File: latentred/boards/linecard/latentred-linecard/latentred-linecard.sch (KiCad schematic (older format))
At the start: 0 parts

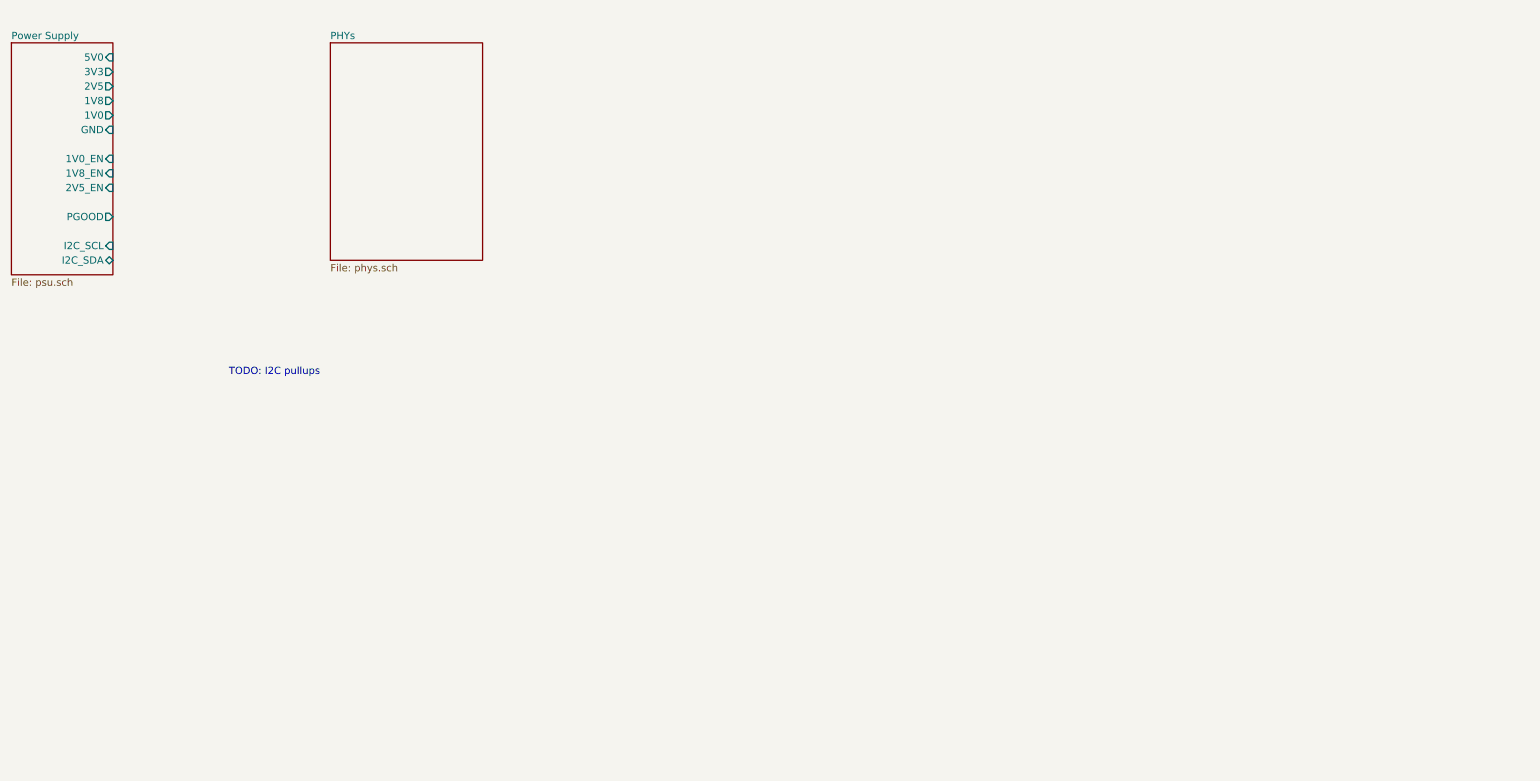
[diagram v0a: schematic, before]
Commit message: Continued work on line card design. Now have PSU and all PHYs, still working on clock distribution.
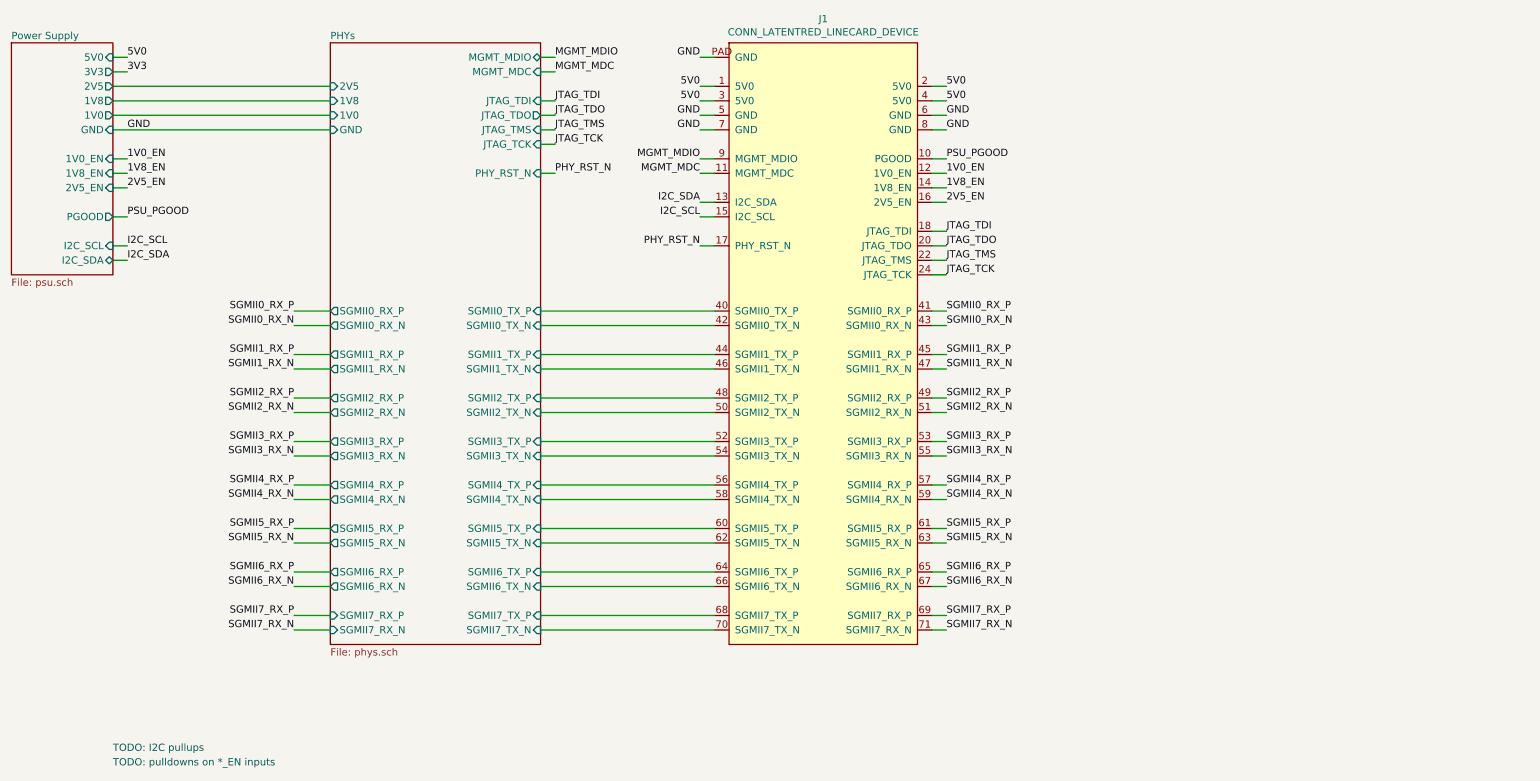
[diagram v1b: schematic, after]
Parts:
- added J1: CONN_LATENTRED_LINECARD_DEVICE, symbol special-azonenberg:CONN_LATENTRED_LINECARD_DEVICE
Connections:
- new net 1V0_EN: J1.12 (1V0_EN)
- new net 1V8_EN: J1.14 (1V8_EN)
- new net 2V5_EN: J1.16 (2V5_EN)
- new net 5V0: J1.1 (5V0), J1.2 (5V0), J1.3 (5V0), J1.4 (5V0)
- new net GND: J1.5 (GND), J1.6 (GND), J1.7 (GND), J1.8 (GND), J1.PAD (GND)
- new net I2C_SCL: J1.15 (I2C_SCL)
- new net I2C_SDA: J1.13 (I2C_SDA)
- new net JTAG_TCK: J1.24 (JTAG_TCK)
- new net JTAG_TDI: J1.18 (JTAG_TDI)
- new net JTAG_TDO: J1.20 (JTAG_TDO)
- new net JTAG_TMS: J1.22 (JTAG_TMS)
- new net MGMT_MDC: J1.11 (MGMT_MDC)
- new net MGMT_MDIO: J1.9 (MGMT_MDIO)
- new net PHY_RST_N: J1.17 (PHY_RST_N)
- new net PHYs/SGMII0_TX_N: J1.42 (SGMII0_TX_N)
- new net PHYs/SGMII0_TX_P: J1.40 (SGMII0_TX_P)
- new net PHYs/SGMII1_TX_N: J1.46 (SGMII1_TX_N)
- new net PHYs/SGMII1_TX_P: J1.44 (SGMII1_TX_P)
- new net PHYs/SGMII2_TX_N: J1.50 (SGMII2_TX_N)
- new net PHYs/SGMII2_TX_P: J1.48 (SGMII2_TX_P)
- new net PHYs/SGMII3_TX_N: J1.54 (SGMII3_TX_N)
- new net PHYs/SGMII3_TX_P: J1.52 (SGMII3_TX_P)
- new net PHYs/SGMII4_TX_N: J1.58 (SGMII4_TX_N)
- new net PHYs/SGMII4_TX_P: J1.56 (SGMII4_TX_P)
- new net PHYs/SGMII5_TX_N: J1.62 (SGMII5_TX_N)
- new net PHYs/SGMII5_TX_P: J1.60 (SGMII5_TX_P)
- new net PHYs/SGMII6_TX_N: J1.66 (SGMII6_TX_N)
- new net PHYs/SGMII6_TX_P: J1.64 (SGMII6_TX_P)
- new net PHYs/SGMII7_TX_N: J1.70 (SGMII7_TX_N)
- new net PHYs/SGMII7_TX_P: J1.68 (SGMII7_TX_P)
- new net PSU_PGOOD: J1.10 (PGOOD)
- new net SGMII0_RX_N: J1.43 (SGMII0_RX_N)
- new net SGMII0_RX_P: J1.41 (SGMII0_RX_P)
- new net SGMII1_RX_N: J1.47 (SGMII1_RX_N)
- new net SGMII1_RX_P: J1.45 (SGMII1_RX_P)
- new net SGMII2_RX_N: J1.51 (SGMII2_RX_N)
- new net SGMII2_RX_P: J1.49 (SGMII2_RX_P)
- new net SGMII3_RX_N: J1.55 (SGMII3_RX_N)
- new net SGMII3_RX_P: J1.53 (SGMII3_RX_P)
- new net SGMII4_RX_N: J1.59 (SGMII4_RX_N)
- new net SGMII4_RX_P: J1.57 (SGMII4_RX_P)
- new net SGMII5_RX_N: J1.63 (SGMII5_RX_N)
- new net SGMII5_RX_P: J1.61 (SGMII5_RX_P)
- new net SGMII6_RX_N: J1.67 (SGMII6_RX_N)
- new net SGMII6_RX_P: J1.65 (SGMII6_RX_P)
- new net SGMII7_RX_N: J1.71 (SGMII7_RX_N)
- new net SGMII7_RX_P: J1.69 (SGMII7_RX_P)
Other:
- note added: "TODO: pulldowns on *_EN inputs"

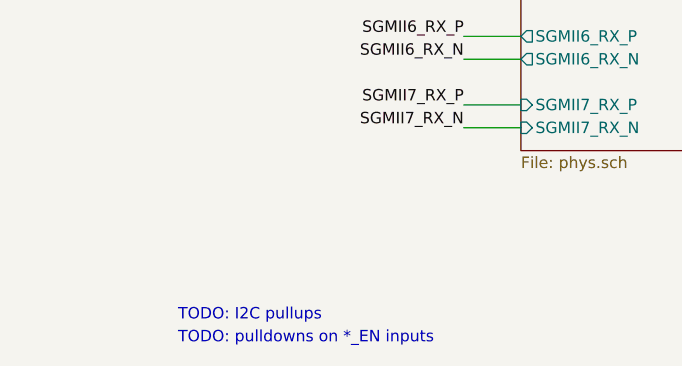
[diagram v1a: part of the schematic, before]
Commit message: Finished initial version of LATENTRED line card schematic. Not yet reviewed.
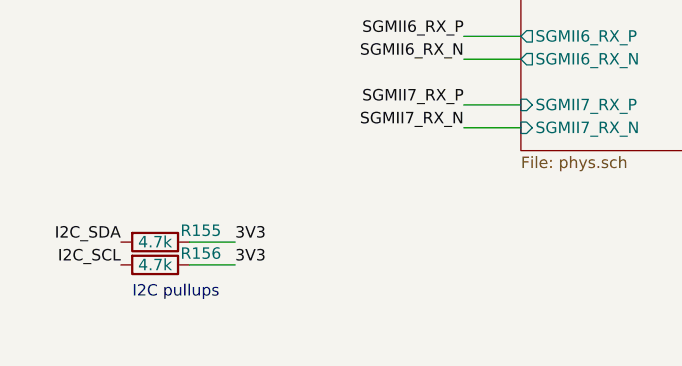
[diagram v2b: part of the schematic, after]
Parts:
- added R155, R156: 4.7k, symbol device:R
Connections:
- net 3V3: now also R155.1, R156.1
- net I2C_SCL: now also R156.2
- net I2C_SDA: now also R155.2
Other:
- note added: "I2C pullups"
- note removed: "TODO: I2C pullups"
- note removed: "TODO: pulldowns on *_EN inputs"
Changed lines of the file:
@@
 F44 "SGMII7_RX_N" I L 3000 4850 50
 $EndSheet
-Text Notes 1500 5700 0    50   ~ 0
-TODO: I2C pullups
+Text Notes 1300 5600 0    50   ~ 0
+I2C pullups
 $Comp
 L special-azonenberg:CONN_LATENTRED_LINECARD_DEVICE J1
@@
 Wire Wire Line
 	1600 1000 1500 1000
-Text Notes 1500 5800 0    50   ~ 0
-TODO: pulldowns on *_EN inputs
 Text Label 4550 900  0    50   ~ 0
 MGMT_MDIO
@@
 Wire Wire Line
 	7150 4850 7250 4850
+$Comp
+L device:R R155
+U 1 1 6910FC55
+P 1400 5350
+F 0 "R155" V 1350 5550 50  0000 C CNN
+F 1 "4.7k" V 1400 5350 50  0000 C CNN
+F 2 "" V 1330 5350 50  0001 C CNN
+F 3 "" H 1400 5350 50  0001 C CNN
+	1    1400 5350
+	0    1    1    0
+$EndComp
+Text Label 1250 5350 2    50   ~ 0
+I2C_SDA
+Text Label 1750 5350 0    50   ~ 0
+3V3
+Wire Wire Line
+	1550 5350 1750 5350
+$Comp
+L device:R R156
+U 1 1 6911860F
+P 1400 5450
+F 0 "R156" V 1350 5650 50  0000 C CNN
+F 1 "4.7k" V 1400 5450 50  0000 C CNN
+F 2 "" V 1330 5450 50  0001 C CNN
+F 3 "" H 1400 5450 50  0001 C CNN
+	1    1400 5450
+	0    1    1    0
+$EndComp
+Text Label 1250 5450 2    50   ~ 0
+I2C_SCL
+Text Label 1750 5450 0    50   ~ 0
+3V3
+Wire Wire Line
+	1550 5450 1750 5450
 $EndSCHEMATC

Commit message: Finished initial footprint creation, ready to begin layout
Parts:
- J1: footprint (none) -> azonenberg_pcb:CONN_SAMTEC_QTH-040-01-L-D-DP-A
- R155, R156: footprint (none) -> azonenberg_pcb:EIA_0402_RES_NOSILK
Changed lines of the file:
@@
 Sheet 1 3
 Title "LATENTRED 8-port 10/100/1000 Base-T Line Card"
-Date "2018-04-17"
+Date "2018-04-18"
 Rev "0.1"
 Comp "Andrew D. Zonenberg"
@@
 F 0 "J1" H 6400 9265 50  0000 C CNN
 F 1 "CONN_LATENTRED_LINECARD_DEVICE" H 6400 9174 50  0000 C CNN
-F 2 "" H 5750 4750 50  0001 C CNN
+F 2 "azonenberg_pcb:CONN_SAMTEC_QTH-040-01-L-D-DP-A" H 5750 4750 50  0001 C CNN
 F 3 "" H 5750 4750 50  0001 C CNN
 	1    5750 4950
@@
 F 0 "R155" V 1350 5550 50  0000 C CNN
 F 1 "4.7k" V 1400 5350 50  0000 C CNN
-F 2 "" V 1330 5350 50  0001 C CNN
+F 2 "azonenberg_pcb:EIA_0402_RES_NOSILK" V 1330 5350 50  0001 C CNN
 F 3 "" H 1400 5350 50  0001 C CNN
 	1    1400 5350
@@
 F 0 "R156" V 1350 5650 50  0000 C CNN
 F 1 "4.7k" V 1400 5450 50  0000 C CNN
-F 2 "" V 1330 5450 50  0001 C CNN
+F 2 "azonenberg_pcb:EIA_0402_RES_NOSILK" V 1330 5450 50  0001 C CNN
 F 3 "" H 1400 5450 50  0001 C CNN
 	1    1400 5450

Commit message: Continued magnetic-and-RJ45 layout
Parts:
- added MH1, MH2, MH3, MH4: HOLE_4_40, azonenberg_pcb:MECHANICAL_CLEARANCEHOLE_4_40, symbol Connector:Conn_01x01
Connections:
- no-connect marks 0 -> 4
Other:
- note added: "TODO: run 5V on the other blade of the QTH-DP"
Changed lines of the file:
@@
 Sheet 1 3
 Title "LATENTRED 8-port 10/100/1000 Base-T Line Card"
-Date "2018-04-18"
+Date "2018-04-21"
 Rev "0.1"
 Comp "Andrew D. Zonenberg"
@@
 Wire Wire Line
 	1550 5450 1750 5450
+$Comp
+L Connector:Conn_01x01 MH1
+U 1 1 6915631E
+P 10500 700
+F 0 "MH1" H 10579 742 50  0000 L CNN
+F 1 "HOLE_4_40" H 10579 651 50  0000 L CNN
+F 2 "azonenberg_pcb:MECHANICAL_CLEARANCEHOLE_4_40" H 10500 700 50  0001 C CNN
+F 3 "~" H 10500 700 50  0001 C CNN
+	1    10500 700
+	1    0    0    -1
+$EndComp
+NoConn ~ 10300 700
+$Comp
+L Connector:Conn_01x01 MH2
+U 1 1 6915AA4F
+P 10500 900
+F 0 "MH2" H 10579 942 50  0000 L CNN
+F 1 "HOLE_4_40" H 10579 851 50  0000 L CNN
+F 2 "azonenberg_pcb:MECHANICAL_CLEARANCEHOLE_4_40" H 10500 900 50  0001 C CNN
+F 3 "~" H 10500 900 50  0001 C CNN
+	1    10500 900
+	1    0    0    -1
+$EndComp
+NoConn ~ 10300 900
+$Comp
+L Connector:Conn_01x01 MH3
+U 1 1 6915F08B
+P 10500 1100
+F 0 "MH3" H 10579 1142 50  0000 L CNN
+F 1 "HOLE_4_40" H 10579 1051 50  0000 L CNN
+F 2 "azonenberg_pcb:MECHANICAL_CLEARANCEHOLE_4_40" H 10500 1100 50  0001 C CNN
+F 3 "~" H 10500 1100 50  0001 C CNN
+	1    10500 1100
+	1    0    0    -1
+$EndComp
+NoConn ~ 10300 1100
+$Comp
+L Connector:Conn_01x01 MH4
+U 1 1 6915F092
+P 10500 1300
+F 0 "MH4" H 10579 1342 50  0000 L CNN
+F 1 "HOLE_4_40" H 10579 1251 50  0000 L CNN
+F 2 "azonenberg_pcb:MECHANICAL_CLEARANCEHOLE_4_40" H 10500 1300 50  0001 C CNN
+F 3 "~" H 10500 1300 50  0001 C CNN
+	1    10500 1300
+	1    0    0    -1
+$EndComp
+NoConn ~ 10300 1300
+Text Notes 9050 2050 0    50   ~ 0
+TODO: run 5V on the other blade of the QTH-DP
 $EndSCHEMATC

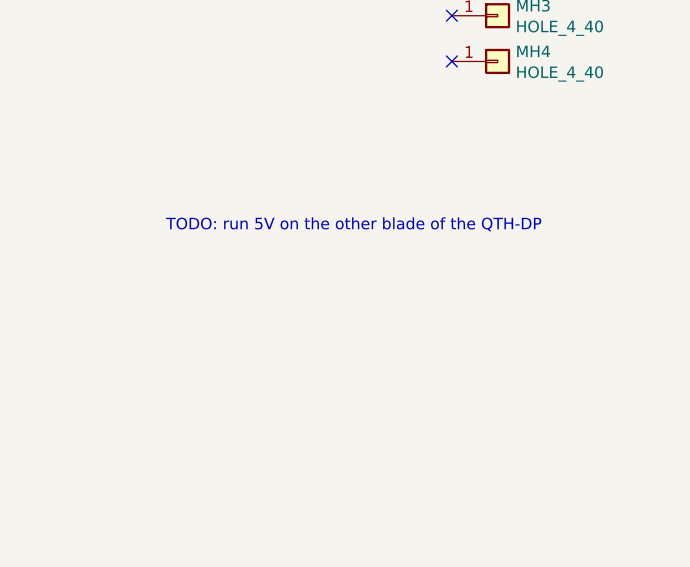
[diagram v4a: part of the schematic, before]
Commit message: Continued initial layout, mostly on PHY indicator LEDs.
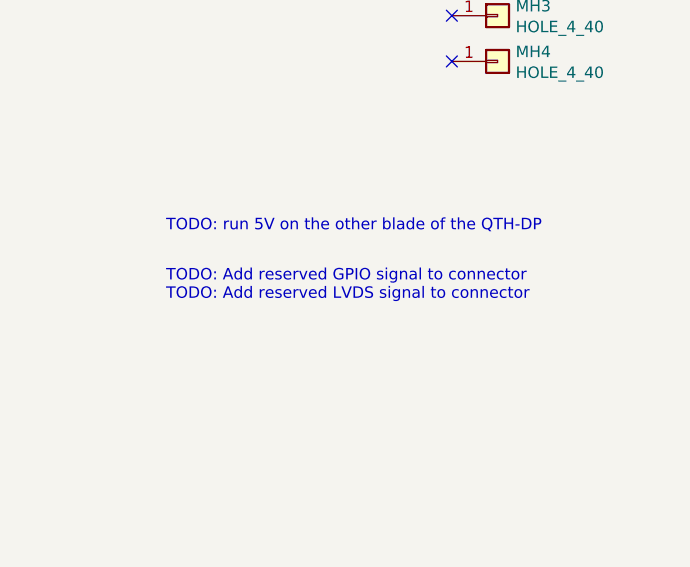
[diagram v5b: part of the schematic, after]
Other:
- note added: "TODO: Add reserved GPIO signal to connector\nTODO: Add reserved LVDS signal to connector"
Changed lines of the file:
@@
 Text Notes 9050 2050 0    50   ~ 0
 TODO: run 5V on the other blade of the QTH-DP
+Text Notes 9050 2350 0    50   ~ 0
+TODO: Add reserved GPIO signal to connector\nTODO: Add reserved LVDS signal to connector
 $EndSCHEMATC

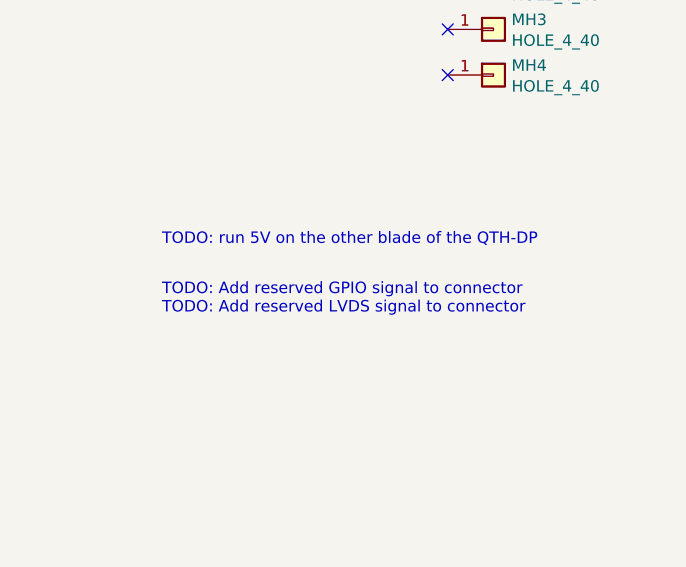
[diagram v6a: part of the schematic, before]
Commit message: Continued PHY layout
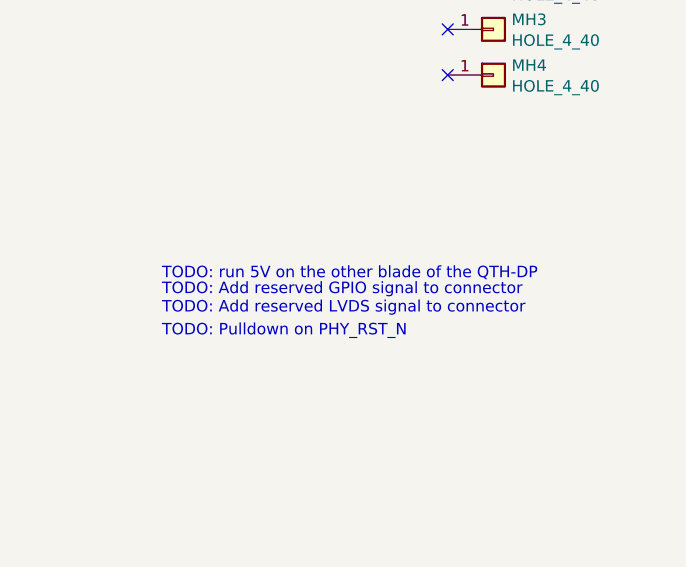
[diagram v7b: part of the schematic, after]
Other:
- note added: "TODO: Pulldown on PHY_RST_N"
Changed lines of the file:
@@
 Sheet 1 3
 Title "LATENTRED 8-port 10/100/1000 Base-T Line Card"
-Date "2018-04-23"
+Date "2018-04-24"
 Rev "0.1"
 Comp "Andrew D. Zonenberg"
@@
 $EndComp
 NoConn ~ 10300 1300
-Text Notes 9050 2050 0    50   ~ 0
+Text Notes 9050 2200 0    50   ~ 0
 TODO: run 5V on the other blade of the QTH-DP
 Text Notes 9050 2350 0    50   ~ 0
 TODO: Add reserved GPIO signal to connector\nTODO: Add reserved LVDS signal to connector
+Text Notes 9050 2450 0    50   ~ 0
+TODO: Pulldown on PHY_RST_N
 $EndSCHEMATC
